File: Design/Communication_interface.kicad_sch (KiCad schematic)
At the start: 68 parts, among them J10 CAN-1, J11 RS-485_2, J12 RS-485_1, J13 CAN_JUM, J14 CAN-2, J9 CAN_JUM, U2 ISO1042BQDWVRQ1, U3 ISO3082DW, U4 ISO3082DW, U5 ISO1042BQDWVRQ1

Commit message: Schematic Design complete
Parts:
- removed J13, J9: CAN_JUM, Connector_PinHeader_2.54mm:PinHeader_1x02_P2.54mm_Vertical, symbol Connector:Conn_01x02_Pin
- added C62: 4700pF, Capacitor_SMD:C_0603_1608Metric_Pad1.08x0.95mm_HandSolder, symbol Device:C
- added R47, R48: 59, Resistor_SMD:R_0603_1608Metric_Pad0.98x0.95mm_HandSolder, symbol Device:R
- added TP13 (x28): TestPoint, TestPoint:TestPoint_Pad_D2.5mm, symbol Connector:TestPoint
- J10, J14: footprint (none) -> TerminalBlock_Phoenix:TerminalBlock_Phoenix_MKDS-1,5-2_1x02_P5.00mm_Horizontal
- J11: renamed from J12; footprint (none) -> TerminalBlock_Phoenix:TerminalBlock_Phoenix_MKDS-1,5-2_1x02_P5.00mm_Horizontal
- J12: renamed from J11; footprint (none) -> TerminalBlock_Phoenix:TerminalBlock_Phoenix_MKDS-1,5-2_1x02_P5.00mm_Horizontal
- L1, L2, L3, L4: footprint (none) -> ACT45B-510-2P-TL003:IND_ACT45R_TDK
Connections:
- net CAN_J is gone; now on net CAN_H: R27.1, R40.1
- net RS-485_1_RX_R is gone; now on net RS-485_1_EN_R: R18.2, U3.3 (R)
- net CAN1_RX_R: now also TP13.1
- net CAN1_TX_R: now also TP13.1
- net CAN2_RX_R: now also TP13.1
- net CAN2_TX_R: now also TP13.1
- net CAN_H: now also R47.1, TP13.1, TP13.1
- net CAN_L: now also R48.2, TP13.1, TP13.1
- net GND1: now also TP13.1, TP13.1, TP13.1, TP13.1
- net GND2: now also C62.2, TP13.1, TP13.1, TP13.1, TP13.1, TP13.1, TP13.1
- net RS-485_1_EN_R: now also TP13.1, TP13.1
- net RS-485_1_TX_R: now also TP13.1
- net RS-485_2_EN_R: now also TP13.1
- net RS-485_2_RX_R: now also TP13.1
- net RS-485_2_TX_R: now also TP13.1
- net RS-485_A: now also TP13.1, TP13.1
- net RS-485_B: now also TP13.1, TP13.1
- new net: C62.1, R47.2, R48.1
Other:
- note added: "Test-Point"
- moved on the sheet: R27, R40

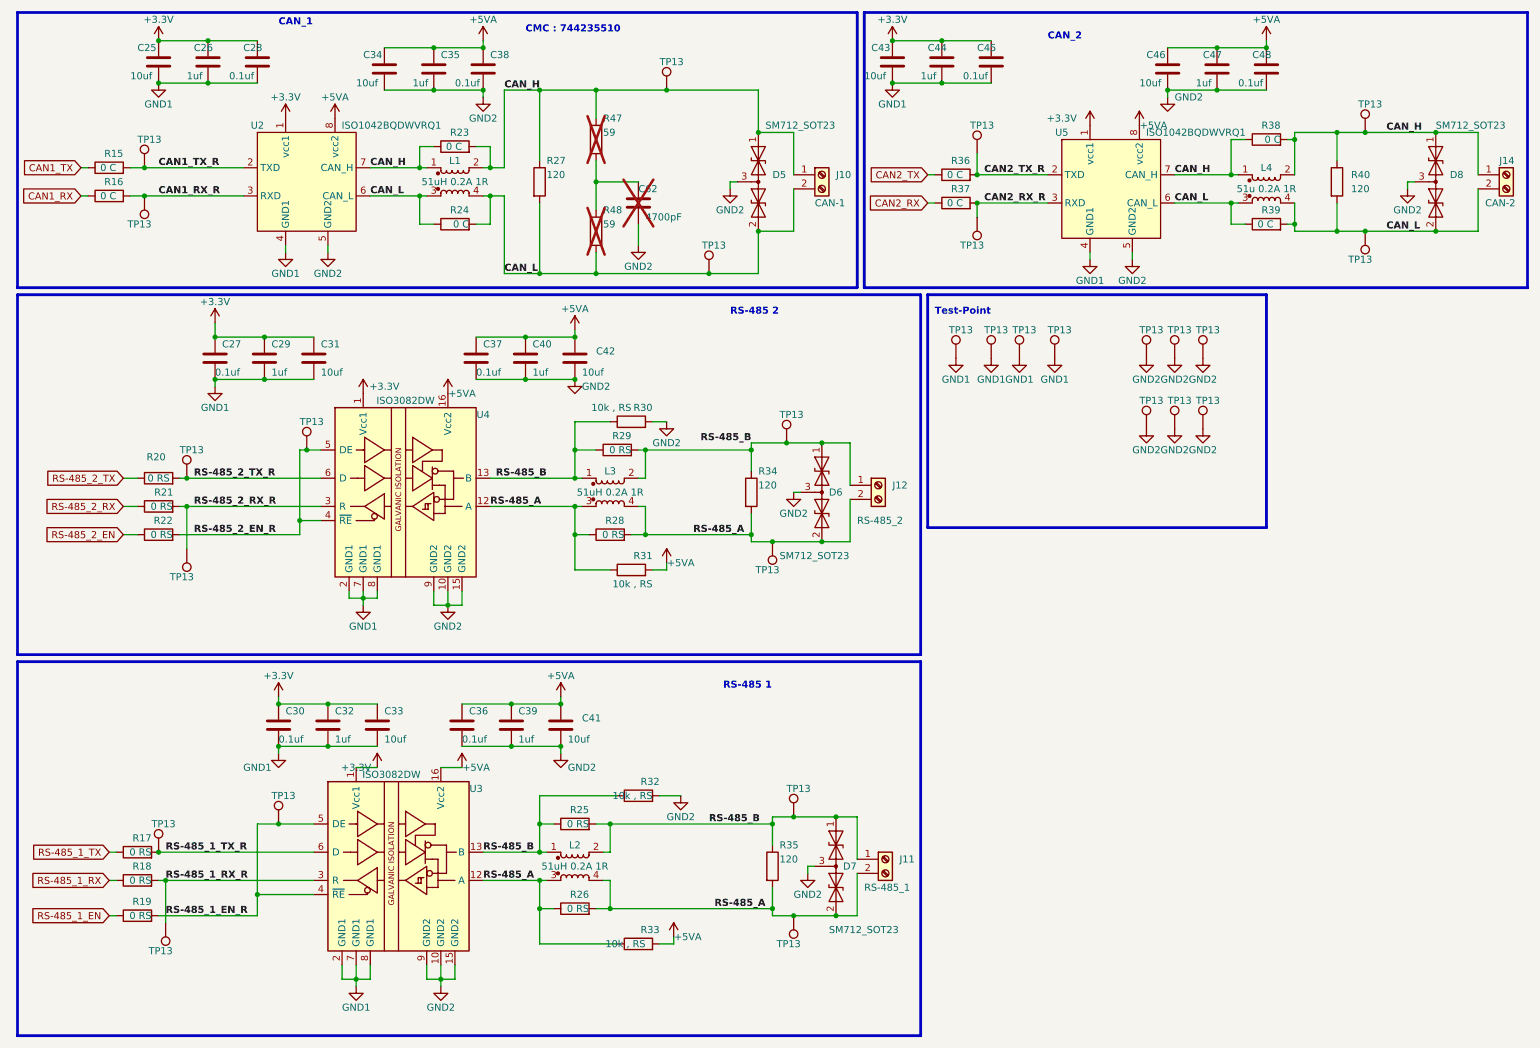
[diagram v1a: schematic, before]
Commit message: PCB design started, comps arranged
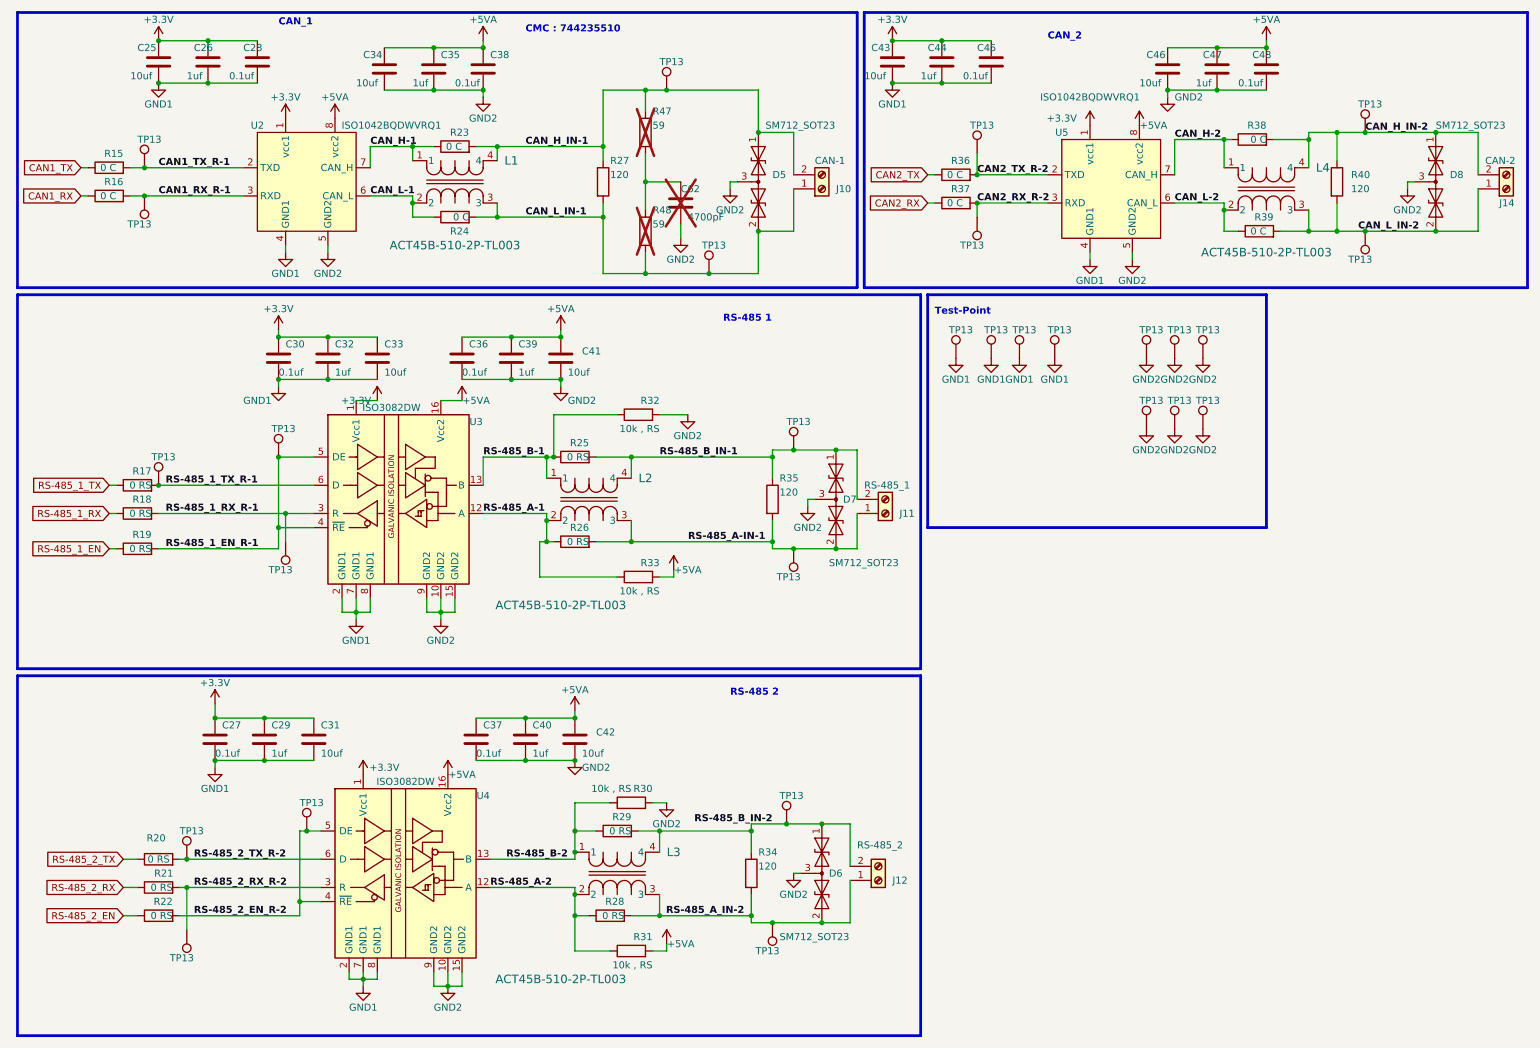
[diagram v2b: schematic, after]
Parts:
- removed L1, L2, L3: 51uH 0.2A 1R, ACT45B-510-2P-TL003:IND_ACT45R_TDK, symbol Device:L_Coupled
- removed L4: 51u 0.2A 1R, ACT45B-510-2P-TL003:IND_ACT45R_TDK, symbol Device:L_Coupled
- added L1, L2, L3, L4: ACT45B-510-2P-TL003, ACT45B-510-2P-TL003:IND_ACT45R_TDK, symbol ACT45B-510-2P-TL003:ACT45B-510-2P-TL003
- TP13: footprint TestPoint:TestPoint_Pad_D2.5mm -> TestPoint:TestPoint_Pad_D1.0mm
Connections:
- net CAN1_RX_R renamed CAN1_RX_R-1
- net CAN1_TX_R renamed CAN1_TX_R-1
- net CAN2_RX_R renamed CAN2_RX_R-2
- net CAN2_TX_R renamed CAN2_TX_R-2
- removed net CAN_H: D5.1 (A1), D8.1 (A1), J10.1 (Pin_1), J14.1 (Pin_1), R23.1, R23.2, R27.1, R38.1, R38.2, R40.1, R47.1, TP13.1, TP13.1, U2.7 (CAN_H), U5.7 (CAN_H)
- removed net CAN_L: D5.2 (A2), D8.2 (A2), J10.2 (Pin_2), J14.2 (Pin_2), R24.1, R24.2, R27.2, R39.1, R39.2, R40.2, R48.2, TP13.1, TP13.1, U2.6 (CAN_L), U5.6 (CAN_L)
- net RS-485_1_EN_R renamed RS-485_1_EN_R-1
- net RS-485_1_EN_R-1: no longer R18.2, TP13.1, U3.3 (R)
- net RS-485_1_TX_R renamed RS-485_1_TX_R-1
- net RS-485_2_EN_R renamed RS-485_2_EN_R-2
- net RS-485_2_RX_R renamed RS-485_2_RX_R-2
- net RS-485_2_TX_R renamed RS-485_2_TX_R-2
- removed net RS-485_A: D6.2 (A2), D7.2 (A2), J11.2 (Pin_2), J12.2 (Pin_2), R26.1, R26.2, R28.1, R28.2, R31.1, R33.1, R34.2, R35.2, TP13.1, TP13.1, U3.12 (A), U4.12 (A)
- removed net RS-485_B: D6.1 (A1), D7.1 (A1), J11.1 (Pin_1), J12.1 (Pin_1), R25.1, R25.2, R29.1, R29.2, R30.1, R32.1, R34.1, R35.1, TP13.1, TP13.1, U3.13 (B), U4.13 (B)
- new net CAN_H-1: L1.1, R23.1, U2.7 (CAN_H)
- new net CAN_H-2: L4.1, R38.1, U5.7 (CAN_H)
- new net CAN_H_IN-1: D5.1 (A1), J10.2 (Pin_2), L1.4, R23.2, R27.1, R47.1, TP13.1
- new net CAN_H_IN-2: D8.1 (A1), J14.2 (Pin_2), L4.4, R38.2, R40.1, TP13.1
- new net CAN_L-1: L1.2, R24.1, U2.6 (CAN_L)
- new net CAN_L-2: L4.2, R39.1, U5.6 (CAN_L)
- new net CAN_L_IN-1: D5.2 (A2), J10.1 (Pin_1), L1.3, R24.2, R27.2, R48.2, TP13.1
- new net CAN_L_IN-2: D8.2 (A2), J14.1 (Pin_1), L4.3, R39.2, R40.2, TP13.1
- new net RS-485_1_RX_R-1: R18.2, TP13.1, U3.3 (R)
- new net RS-485_A-1: L2.2, R26.1, R33.1, U3.12 (A)
- new net RS-485_A-2: L3.2, R28.1, R31.1, U4.12 (A)
- new net RS-485_A-IN-1: D7.2 (A2), J11.1 (Pin_1), L2.3, R26.2, R35.2, TP13.1
- new net RS-485_A_IN-2: D6.2 (A2), J12.1 (Pin_1), L3.3, R28.2, R34.2, TP13.1
- new net RS-485_B-1: L2.1, R25.1, R32.1, U3.13 (B)
- new net RS-485_B-2: L3.1, R29.1, R30.1, U4.13 (B)
- new net RS-485_B_IN-1: D7.1 (A1), J11.2 (Pin_2), L2.4, R25.2, R35.1, TP13.1
- new net RS-485_B_IN-2: D6.1 (A1), J12.2 (Pin_2), L3.4, R29.2, R34.1, TP13.1
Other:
- moved on the sheet: C27, C29, C30, C31, C32, C33, C36, C37, C39, C40, C41, C42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

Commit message: Temp complete of communication section , added Safety caps
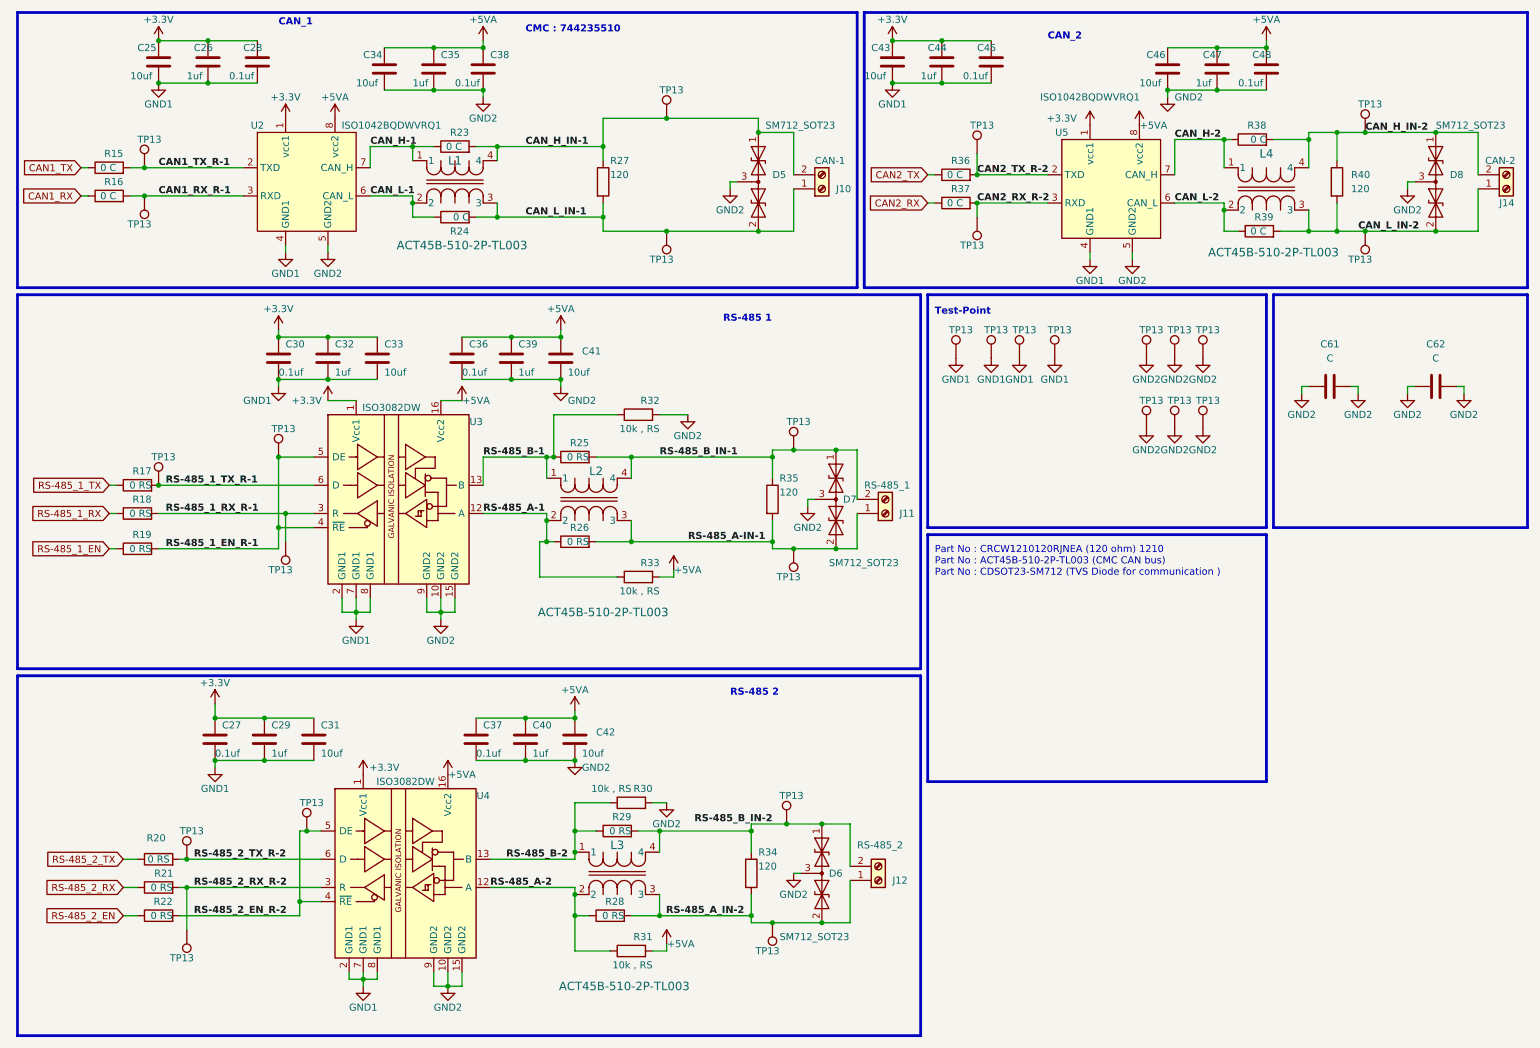
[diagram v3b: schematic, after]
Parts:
- removed R47, R48: 59, Resistor_SMD:R_0603_1608Metric_Pad0.98x0.95mm_HandSolder, symbol Device:R
- added C61: C, symbol Device:C
- C62: value 4700pF -> C; footprint Capacitor_SMD:C_0603_1608Metric_Pad1.08x0.95mm_HandSolder -> (none); now fitted
- R15, R16, R17, R18, R19, R20, R21, R22, R23, R24, R25, R26, R28, R29, R36, R37, R38, R39: footprint Resistor_SMD:R_0603_1608Metric_Pad0.98x0.95mm_HandSolder -> Resistor_SMD:R_0805_2012Metric_Pad1.20x1.40mm_HandSolder
- R27, R34, R35, R40: footprint Resistor_SMD:R_0805_2012Metric_Pad1.20x1.40mm_HandSolder -> Resistor_SMD:R_2512_6332Metric_Pad1.40x3.35mm_HandSolder
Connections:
- net GND2: now also C62.1, C61.1, C61.2
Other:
- note added: "Part No : CRCW1210120RJNEA (120 ohm) 1210 Part No : ACT45B-510-2P-TL003 (CMC CAN bus) Part No : CDSOT23-SM712 (TVS Diode for communication )"
- moved on the sheet: TP13

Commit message: Added lib folder, Layer layed
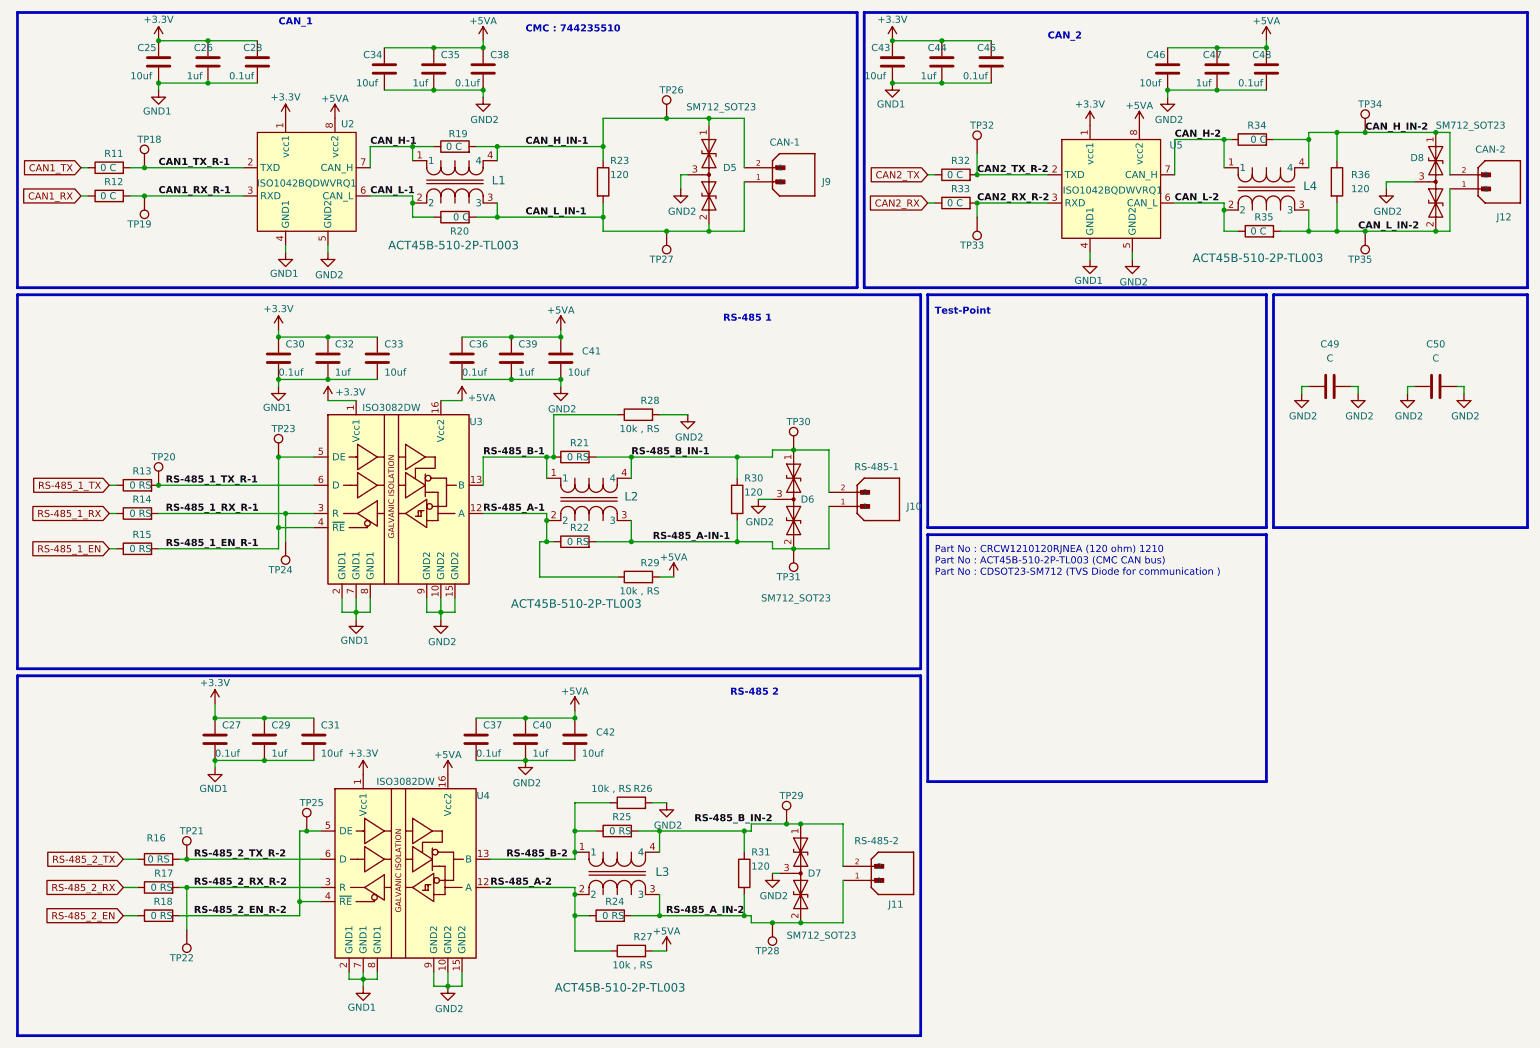
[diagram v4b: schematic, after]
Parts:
- removed J10: CAN-1, TerminalBlock_Phoenix:TerminalBlock_Phoenix_MKDS-1,5-2_1x02_P5.00mm_Horizontal, symbol Connector:Screw_Terminal_01x02
- removed J11: RS-485_1, TerminalBlock_Phoenix:TerminalBlock_Phoenix_MKDS-1,5-2_1x02_P5.00mm_Horizontal, symbol Connector:Screw_Terminal_01x02
- removed J12: RS-485_2, TerminalBlock_Phoenix:TerminalBlock_Phoenix_MKDS-1,5-2_1x02_P5.00mm_Horizontal, symbol Connector:Screw_Terminal_01x02
- removed J14: CAN-2, TerminalBlock_Phoenix:TerminalBlock_Phoenix_MKDS-1,5-2_1x02_P5.00mm_Horizontal, symbol Connector:Screw_Terminal_01x02
- removed TP13 (x10): TestPoint, TestPoint:TestPoint_Pad_D1.0mm, symbol Connector:TestPoint
- added J10: RS-485-1, 0530480210_2pin_P1.25_PicoBlade:MOLEX_530480210, symbol 0530480210_2pin_P1.25_PicoBlade:530480210
- added J11: RS-485-2, 0530480210_2pin_P1.25_PicoBlade:MOLEX_530480210, symbol 0530480210_2pin_P1.25_PicoBlade:530480210
- added J12: CAN-2, 0530480210_2pin_P1.25_PicoBlade:MOLEX_530480210, symbol 0530480210_2pin_P1.25_PicoBlade:530480210
- added J9: CAN-1, 0530480210_2pin_P1.25_PicoBlade:MOLEX_530480210, symbol 0530480210_2pin_P1.25_PicoBlade:530480210
- renumbered C61 to C49, C62 to C50, D7 to D6, D6 to D7, R15 to R11, R16 to R12, R17 to R13, R18 to R14, R19 to R15, R20 to R16, R21 to R17, R22 to R18, R23 to R19, R24 to R20, R25 to R21, R26 to R22, R27 to R23, R28 to R24, R29 to R25, R30 to R26, R31 to R27, R32 to R28, R33 to R29, R35 to R30, R34 to R31, R36 to R32, R37 to R33, R38 to R34, R39 to R35, R40 to R36, TP13 to TP18, TP13 to TP19, TP13 to TP20, TP13 to TP21, TP13 to TP22, TP13 to TP23, TP13 to TP24, TP13 to TP25, TP13 to TP26, TP13 to TP27, TP13 to TP28, TP13 to TP29, TP13 to TP30, TP13 to TP31, TP13 to TP32, TP13 to TP33, TP13 to TP34, TP13 to TP35
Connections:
- net CAN_H_IN-1: now also J9.2
- net CAN_H_IN-2: now also J12.2
- net CAN_L_IN-1: now also J9.1
- net CAN_L_IN-2: now also J12.1
- net RS-485_A-IN-1: now also J10.1
- net RS-485_A_IN-2: now also J11.1
- net RS-485_B_IN-1: now also J10.2
- net RS-485_B_IN-2: now also J11.2
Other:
- moved on the sheet: D5, D6, D7, R30, R31

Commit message: Added everything
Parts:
- added G1: High_Voltage_Warning, High_Voltage_Warning_logo:High_Voltage_Warning, symbol High_Voltage_Warning:HIgh_Voltage_Warning
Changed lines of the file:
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@@
 		(title "Rapid-Core")
 		(date "2024-09-09")
-		(rev "1.0.0")
+		(rev "1.0.1")
 	)
 	(junction
@@
 					(unit 1)
 				)
+			)
+		)
+	)
+	(symbol
+		(lib_id "High_Voltage_Warning:HIgh_Voltage_Warning")
+		(at 190.5 120.65 0)
+		(unit 1)
+		(exclude_from_sim no)
+		(in_bom yes)
+		(on_board yes)
+		(dnp no)
+		(fields_autoplaced yes)
+		(property "Reference" "G1"
+			(at 194.31 120.657 0)
+			(effects
+				(font
+					(size 1.27 1.27)
+				)
+				(justify left)
+			)
+		)
+		(property "Value" "High_Voltage_Warning"
+			(at 185.674 121.158 0)
+			(effects
+				(font
+					(size 1.27 1.27)
+				)
+				(hide yes)
+			)
+		)
+		(property "Footprint" "High_Voltage_Warning_logo:High_Voltage_Warning"
+			(at 190.754 125.73 0)
+			(effects
+				(font
+					(size 1.27 1.27)
+				)
+				(hide yes)
+			)
+		)
+		(property "Datasheet" ""
+			(at 190.5 120.65 0)
+			(effects
+				(font
+					(size 1.27 1.27)
+				)
+				(hide yes)
+			)
+		)
+		(property "Description" ""
+			(at 190.5 120.65 0)
+			(effects
+				(font
+					(size 1.27 1.27)
+				)
+				(hide yes)
+			)
+		)
+		(instances
+			(project ""
+				(path "/1a5d67a4-b410-4c7a-b64e-9e0193c8e6b4/f55b0938-7500-4e0b-96b5-fde9faeb9ba0"
+					(reference "G1")
+					(unit 1)
+				)
